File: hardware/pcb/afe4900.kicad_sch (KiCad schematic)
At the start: 9 parts, among them J4 PPG, U6 AFE4900YZR

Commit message: Use official CAD and shrink the hw_v1 board to 37x30 mm.
Replace the hand-drawn AFE4900, AD5940, ADS1292R, AS7341, MLX90632,
TMP117, LSM6DSV80X, and MCP73831 symbols and footprints with the
SnapMagic and Ultra Librarian libraries. ADS1292R is now the QFN-32
ADS1292RIRSMT, and MLX90632SLD-DCB-100-SP moves SDA/SCL onto the
existing 1.8 V bus. Pin headers and mounting holes are flat solder
pads. The unrouted 4-layer placement keeps the antenna on the left
edge and the skin sensors together on the bottom.

Co-authored-by: Riyu-D1 <Riyu-D1@users.noreply.github.com>
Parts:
- J4: value PPG -> PPG pads; footprint Connector_PinHeader_1.27mm:PinHeader_1x06_P1.27mm_Horizontal -> vitalq:Pads_PPG
- U6: footprint vitalq:AFE4900YZR -> snap:BGA30N40P5X6_260X210X50
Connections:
- no-connect marks 9 -> 10
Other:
- note added: "J4 solder pads, off-board LED and PD. No header."
- note added: "R10 holds CLK low so the internal clock is used. Ball names are the SnapMagic symbol."
- note removed: "ECG pins, TX4, the second photodiode pair, RLD_OUT and PROG_OUT1 are open."
- note removed: "Footprint is hand-drawn from SBAS861B page 5. The public PDF has no ball list."
- note removed: "J4 off-board LED and PD"
- note removed: "R10 holds CLK low so the internal clock is used. Confirm against the full AFE4900 pin table."

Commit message: Pack the hw_v1 board to 36.2 x 28 mm and correct the 3D models.
The LSM6 body is a 3.0 x 2.5 x 0.83 mm box in KiCad VRML units, and the other vendor models are rotated so they stand on their lands. Skin sensors sit in one bottom cluster with the electrode pads around them, bypass parts are packed next to their ICs outside the antenna keep-out, and the schematic frames clear the title block.

Co-authored-by: Riyu-D1 <Riyu-D1@users.noreply.github.com>
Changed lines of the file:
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@@
 		(instances
 			(project "vitalq_hw_v1"
-				(path "/3a03f3a2-f664-49ab-a6e3-0e34faafa582/1e955221-8a59-4a72-bd26-6dbe9ab10b2d"
+				(path "/6fcf6b13-4a8e-4f25-a8b9-d34cb547168d/197eb80f-de84-4da9-b1b6-3c344e51c954"
 					(reference "U6")
 					(unit 1)
@@
 		(instances
 			(project "vitalq_hw_v1"
-				(path "/3a03f3a2-f664-49ab-a6e3-0e34faafa582/1e955221-8a59-4a72-bd26-6dbe9ab10b2d"
+				(path "/6fcf6b13-4a8e-4f25-a8b9-d34cb547168d/197eb80f-de84-4da9-b1b6-3c344e51c954"
 					(reference "J4")
 					(unit 1)
@@
 		(instances
 			(project "vitalq_hw_v1"
-				(path "/3a03f3a2-f664-49ab-a6e3-0e34faafa582/1e955221-8a59-4a72-bd26-6dbe9ab10b2d"
+				(path "/6fcf6b13-4a8e-4f25-a8b9-d34cb547168d/197eb80f-de84-4da9-b1b6-3c344e51c954"
 					(reference "C11")
 					(unit 1)
@@
 		(instances
 			(project "vitalq_hw_v1"
-				(path "/3a03f3a2-f664-49ab-a6e3-0e34faafa582/1e955221-8a59-4a72-bd26-6dbe9ab10b2d"
+				(path "/6fcf6b13-4a8e-4f25-a8b9-d34cb547168d/197eb80f-de84-4da9-b1b6-3c344e51c954"
 					(reference "#PWR038")
 					(unit 1)
@@
 		(instances
 			(project "vitalq_hw_v1"
-				(path "/3a03f3a2-f664-49ab-a6e3-0e34faafa582/1e955221-8a59-4a72-bd26-6dbe9ab10b2d"
+				(path "/6fcf6b13-4a8e-4f25-a8b9-d34cb547168d/197eb80f-de84-4da9-b1b6-3c344e51c954"
 					(reference "#PWR039")
 					(unit 1)
@@
 		(instances
 			(project "vitalq_hw_v1"
-				(path "/3a03f3a2-f664-49ab-a6e3-0e34faafa582/1e955221-8a59-4a72-bd26-6dbe9ab10b2d"
+				(path "/6fcf6b13-4a8e-4f25-a8b9-d34cb547168d/197eb80f-de84-4da9-b1b6-3c344e51c954"
 					(reference "C12")
 					(unit 1)
@@
 		(instances
 			(project "vitalq_hw_v1"
-				(path "/3a03f3a2-f664-49ab-a6e3-0e34faafa582/1e955221-8a59-4a72-bd26-6dbe9ab10b2d"
+				(path "/6fcf6b13-4a8e-4f25-a8b9-d34cb547168d/197eb80f-de84-4da9-b1b6-3c344e51c954"
 					(reference "#PWR040")
 					(unit 1)
@@
 		(instances
 			(project "vitalq_hw_v1"
-				(path "/3a03f3a2-f664-49ab-a6e3-0e34faafa582/1e955221-8a59-4a72-bd26-6dbe9ab10b2d"
+				(path "/6fcf6b13-4a8e-4f25-a8b9-d34cb547168d/197eb80f-de84-4da9-b1b6-3c344e51c954"
 					(reference "#PWR041")
 					(unit 1)
@@
 		(instances
 			(project "vitalq_hw_v1"
-				(path "/3a03f3a2-f664-49ab-a6e3-0e34faafa582/1e955221-8a59-4a72-bd26-6dbe9ab10b2d"
+				(path "/6fcf6b13-4a8e-4f25-a8b9-d34cb547168d/197eb80f-de84-4da9-b1b6-3c344e51c954"
 					(reference "C13")
 					(unit 1)
@@
 		(instances
 			(project "vitalq_hw_v1"
-				(path "/3a03f3a2-f664-49ab-a6e3-0e34faafa582/1e955221-8a59-4a72-bd26-6dbe9ab10b2d"
+				(path "/6fcf6b13-4a8e-4f25-a8b9-d34cb547168d/197eb80f-de84-4da9-b1b6-3c344e51c954"
 					(reference "#PWR042")
 					(unit 1)
@@
 		(instances
 			(project "vitalq_hw_v1"
-				(path "/3a03f3a2-f664-49ab-a6e3-0e34faafa582/1e955221-8a59-4a72-bd26-6dbe9ab10b2d"
+				(path "/6fcf6b13-4a8e-4f25-a8b9-d34cb547168d/197eb80f-de84-4da9-b1b6-3c344e51c954"
 					(reference "#PWR043")
 					(unit 1)
@@
 		(instances
 			(project "vitalq_hw_v1"
-				(path "/3a03f3a2-f664-49ab-a6e3-0e34faafa582/1e955221-8a59-4a72-bd26-6dbe9ab10b2d"
+				(path "/6fcf6b13-4a8e-4f25-a8b9-d34cb547168d/197eb80f-de84-4da9-b1b6-3c344e51c954"
 					(reference "C14")
 					(unit 1)
@@
 		(instances
 			(project "vitalq_hw_v1"
-				(path "/3a03f3a2-f664-49ab-a6e3-0e34faafa582/1e955221-8a59-4a72-bd26-6dbe9ab10b2d"
+				(path "/6fcf6b13-4a8e-4f25-a8b9-d34cb547168d/197eb80f-de84-4da9-b1b6-3c344e51c954"
 					(reference "#PWR044")
 					(unit 1)
@@
 		(instances
 			(project "vitalq_hw_v1"
-				(path "/3a03f3a2-f664-49ab-a6e3-0e34faafa582/1e955221-8a59-4a72-bd26-6dbe9ab10b2d"
+				(path "/6fcf6b13-4a8e-4f25-a8b9-d34cb547168d/197eb80f-de84-4da9-b1b6-3c344e51c954"
 					(reference "C15")
 					(unit 1)
@@
 		(instances
 			(project "vitalq_hw_v1"
-				(path "/3a03f3a2-f664-49ab-a6e3-0e34faafa582/1e955221-8a59-4a72-bd26-6dbe9ab10b2d"
+				(path "/6fcf6b13-4a8e-4f25-a8b9-d34cb547168d/197eb80f-de84-4da9-b1b6-3c344e51c954"
 					(reference "#PWR045")
 					(unit 1)
@@
 		(instances
 			(project "vitalq_hw_v1"
-				(path "/3a03f3a2-f664-49ab-a6e3-0e34faafa582/1e955221-8a59-4a72-bd26-6dbe9ab10b2d"
+				(path "/6fcf6b13-4a8e-4f25-a8b9-d34cb547168d/197eb80f-de84-4da9-b1b6-3c344e51c954"
 					(reference "R9")
 					(unit 1)
@@
 		(instances
 			(project "vitalq_hw_v1"
-				(path "/3a03f3a2-f664-49ab-a6e3-0e34faafa582/1e955221-8a59-4a72-bd26-6dbe9ab10b2d"
+				(path "/6fcf6b13-4a8e-4f25-a8b9-d34cb547168d/197eb80f-de84-4da9-b1b6-3c344e51c954"
 					(reference "#PWR046")
 					(unit 1)
@@
 		(instances
 			(project "vitalq_hw_v1"
-				(path "/3a03f3a2-f664-49ab-a6e3-0e34faafa582/1e955221-8a59-4a72-bd26-6dbe9ab10b2d"
+				(path "/6fcf6b13-4a8e-4f25-a8b9-d34cb547168d/197eb80f-de84-4da9-b1b6-3c344e51c954"
 					(reference "R10")
 					(unit 1)
@@
 		(instances
 			(project "vitalq_hw_v1"
-				(path "/3a03f3a2-f664-49ab-a6e3-0e34faafa582/1e955221-8a59-4a72-bd26-6dbe9ab10b2d"
+				(path "/6fcf6b13-4a8e-4f25-a8b9-d34cb547168d/197eb80f-de84-4da9-b1b6-3c344e51c954"
 					(reference "#PWR047")
 					(unit 1)
@@
 	)
 	(rectangle
-		(start 12.0 18.0)
-		(end 408.0 248.0)
+		(start 12.0 40.0)
+		(end 406.0 248.0)
 		(stroke (width 0.4) (type dash))
 		(fill (type none))

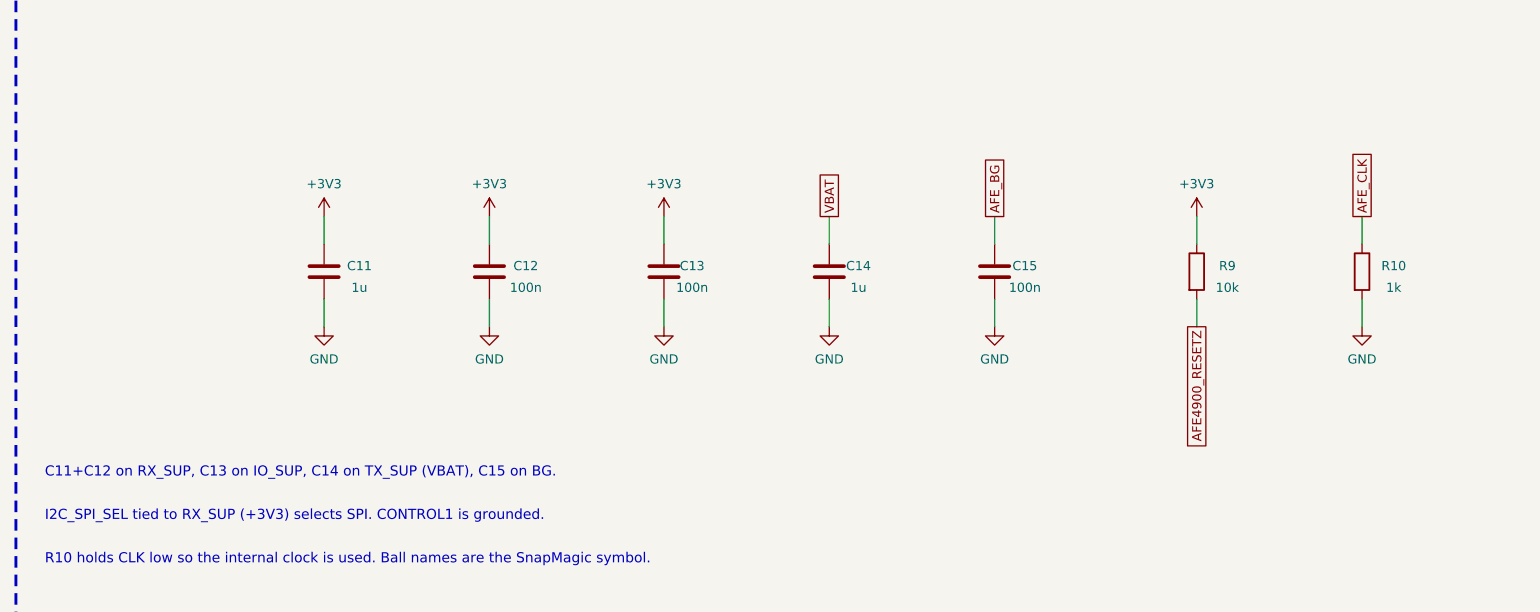
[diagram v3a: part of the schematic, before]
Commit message: Seat the QFN models and drop passives the datasheets do not require.
The ADS1292R STEP is already Z-up, so the extra X rotation stood the
4x4x1 mm body on edge. Remove TP1, TP2, C5, C12, C17, C31 and R4, add
the 1 uF AVDD bulk capacitor, and shorten the outline to 36.2 x 27.8 mm.

Co-authored-by: Riyu-D1 <Riyu-D1@users.noreply.github.com>
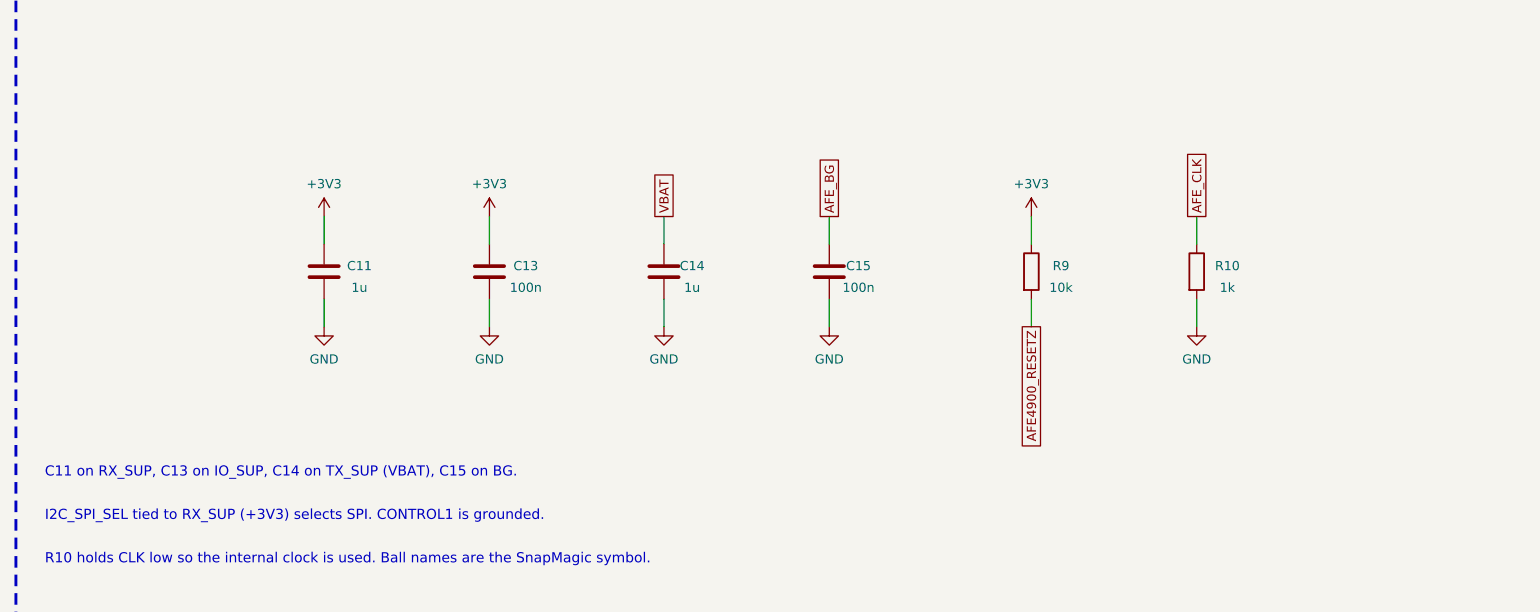
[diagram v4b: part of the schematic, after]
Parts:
- removed C12: 100n, Capacitor_SMD:C_0402_1005Metric, symbol vitalq:C
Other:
- note added: "C11 on RX_SUP, C13 on IO_SUP, C14 on TX_SUP (VBAT), C15 on BG."
- note removed: "C11+C12 on RX_SUP, C13 on IO_SUP, C14 on TX_SUP (VBAT), C15 on BG."

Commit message: Add the chest-board sensors and replace the 3.3 V LDO with a TPS63802.
The unrouted 40 x 34 mm board keeps every previous part except the off-board PPG pads, which the SFH 7072 replaces. Respiration, a second ECG lead, electrode protection, EDA, fuel gauge, flash, and the I/O expander are in the schematic.

Co-authored-by: Riyu-D1 <Riyu-D1@users.noreply.github.com>
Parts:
- removed J4: PPG pads, vitalq:Pads_PPG, symbol vitalq:Conn_01x06_Pin
- added C46: 2.2u, Capacitor_SMD:C_0402_1005Metric, symbol vitalq:C
- added C47: 4.7u, Capacitor_SMD:C_0603_1608Metric, symbol vitalq:C
- added C56, C57: 100n, Capacitor_SMD:C_0402_1005Metric, symbol vitalq:C
- added L2: 1.0u, vitalq:L_DFE201612E, symbol vitalq:L
- added R25: 100k, Resistor_SMD:R_0402_1005Metric, symbol vitalq:R
- added R43, R44, R45, R46: 10M, Resistor_SMD:R_0402_1005Metric, symbol vitalq:R
- added U15: TPS61240YFFR, vitalq:TPS61240_YFF, symbol vitalq:TPS61240
- added U16: SFH 7072, vitalq:SFH7072, symbol vitalq:SFH7072
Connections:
- net +3V3: now also R43.1, R45.1; no longer R9.1
- net AFE4900_RESETZ: now also R9.1; no longer R9.2
- net GND: now also R9.2, C46.2, C47.2, R25.2, R44.2, R46.2, U15.A2 (GND)
- net PD_INM: now also U16.2 (PD1_A)
- net PD_INP: now also U16.1 (PD1_C)
- net TX1: now also U16.6 (G1_C)
- net TX2: now also U16.12 (G2_C)
- net TX3: now also U16.8 (R_C)
- net VBAT: now also C46.1, U15.A1 (VIN); no longer C14.1, U6.F5 (TX_SUP)
- net AFE_INM: now reaches U6.A1 (INM_ECG)
- net AFE_INM: now also C57.2, R45.2, R46.1
- net AFE_INP: now reaches U6.B1 (INP_ECG)
- net AFE_INP: now also C56.2, R43.2, R44.1
- net PD2_INP: now reaches U6.B2 (INP2)
- net PD2_INP: now also U16.3 (PD2_C)
- net PD2_INM: now reaches U6.B3 (INM2)
- net PD2_INM: now also U16.10 (PD2_A)
- net TX4: now reaches U6.C5 (TX4)
- net TX4: now also U16.9 (IR_C)
- new net AFE_N_AC: C57.1
- new net AFE_P_AC: C56.1
- new net TX5_EN: R25.1, U15.C1 (EN)
- new net TX_5V: C14.1, C47.1, L2.2, U15.B2 (VOUT), U15.C2 (FB), U16.11 (G2_A), U16.4 (IR_A), U16.5 (G1_A), U16.7 (R_A), U6.F5 (TX_SUP)
- new net TX_SW: L2.1, U15.B1 (L)
- no-connect marks 10 -> 5
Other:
- note added: "AFE4900 PPG and second ECG lead"
- note added: "C11 RX_SUP, C13 IO_SUP, C14 local TX_SUP, C47 is the boost 4.7 uF. C15 is BG."
- note added: "R9 holds RESETZ down until the expander drives it. R10 holds CLK low. AFE RLD_OUT is open."
- note added: "SFH 7072 is on the board. TX_SUP is the TPS61240 5 V boost. AFE RLD is unused."
- note removed: "1 VBAT (TX_SUP)"
- note removed: "2 TX1 3 TX2 4 TX3"
- note removed: "5 PD cathode (INP)"
- note removed: "6 PD anode (INM)"
- note removed: "AFE4900 PPG"
- note removed: "C11 on RX_SUP, C13 on IO_SUP, C14 on TX_SUP (VBAT), C15 on BG."
- note removed: "I2C_SPI_SEL tied to RX_SUP (+3V3) selects SPI. CONTROL1 is grounded."
- note removed: "J4 solder pads, off-board LED and PD. No header."
- note removed: "R10 holds CLK low so the internal clock is used. Ball names are the SnapMagic symbol."
- note removed: "SPI mode. LED and photodiode are off the board, on J4. No on-board optics."
